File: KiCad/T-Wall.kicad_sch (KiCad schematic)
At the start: 62 parts, among them J1 IDC, J10 Conn_01x13, J2 IDC, J3 IDC, J4 IDC, J5 IDC, J6 IDC, J7 IDC, J8 IDC, J9 2086-1107/300-000/997-607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

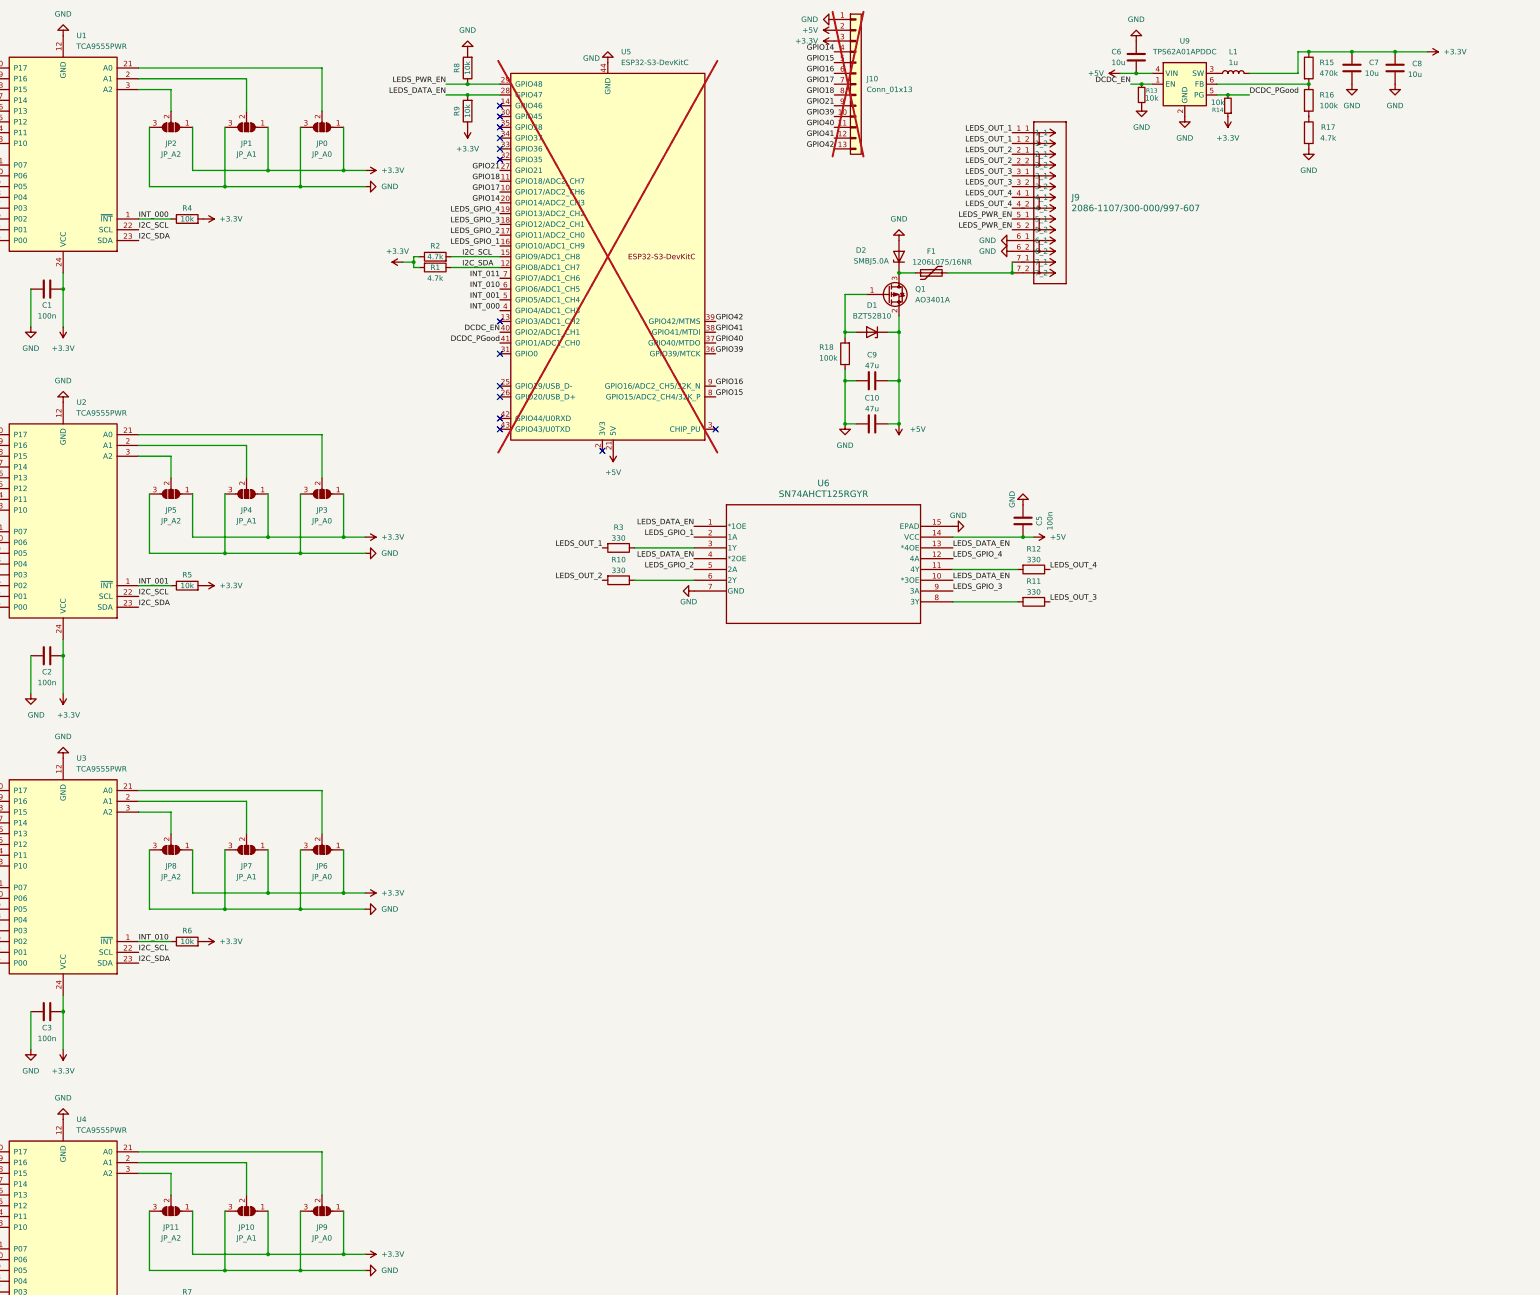
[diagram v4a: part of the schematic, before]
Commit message: PCB: finished for purchase at JLCPCB
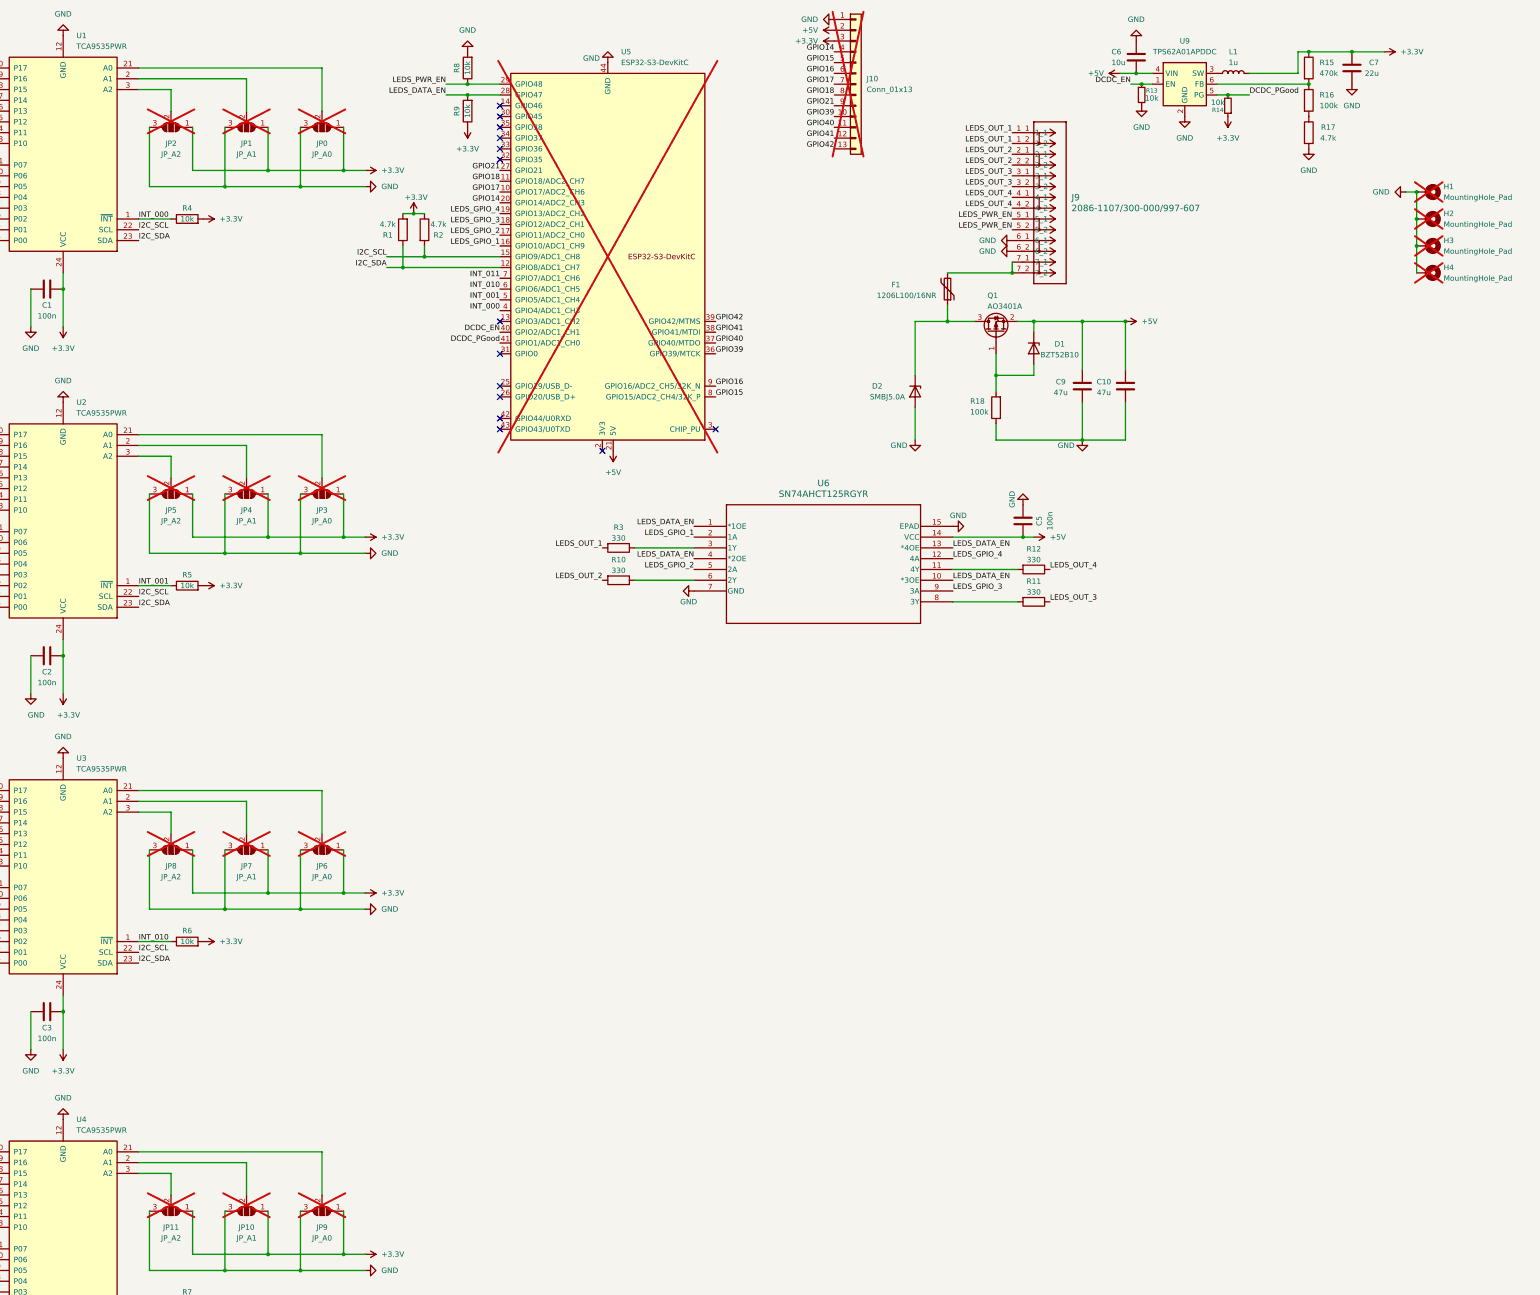
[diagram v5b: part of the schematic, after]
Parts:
- removed C8: 10u, Capacitor_SMD:C_1206_3216Metric_Pad1.33x1.80mm_HandSolder, symbol Device:C
- removed U1, U2, U3, U4: TCA9555PWR, Package_SO:TSSOP-24_4.4x7.8mm_P0.65mm, symbol Interface_Expansion:TCA9555PWR
- added H1, H2, H3, H4: MountingHole_Pad, MountingHole:MountingHole_3.2mm_M3_Pad_Via, symbol Mechanical:MountingHole_Pad
- added U1, U2, U3, U4: TCA9535PWR, Package_SO:TSSOP-24_4.4x7.8mm_P0.65mm, symbol Interface_Expansion:TCA9535PWR
- C7: value 10u -> 22u; LCSC C13585 -> C12891
- F1: value 1206L075/16NR -> 1206L100/16NR; LCSC C7542951 -> C7542956
- JP0, JP1, JP10, JP11, JP2, JP3, JP4, JP5, JP6, JP7, JP8, JP9: now not fitted
- L1: LCSC C1042 -> C6364732
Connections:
- net +3.3V: now also U1.24 (VCC), U2.24 (VCC), U3.24 (VCC), U4.24 (VCC)
- net GND: now also H1.1, H2.1, H3.1, H4.1, U1.12 (GND), U2.12 (GND), U3.12 (GND), U4.12 (GND)
- net I2C_SCL: now also U1.22 (SCL), U2.22 (SCL), U3.22 (SCL), U4.22 (SCL)
- net I2C_SDA: now also U1.23 (SDA), U2.23 (SDA), U3.23 (SDA), U4.23 (SDA)
- net INT_000: now also U1.1 (~{INT})
- net INT_001: now also U2.1 (~{INT})
- net INT_010: now also U3.1 (~{INT})
- net INT_011: now also U4.1 (~{INT})
- net Sensor_R1S1: now also U1.4 (P00)
- net Sensor_R1S2: now also U1.5 (P01)
- net Sensor_R1S3: now also U1.6 (P02)
- net Sensor_R1S4: now also U1.7 (P03)
- net Sensor_R1S5: now also U1.8 (P04)
- net Sensor_R1S6: now also U1.9 (P05)
- net Sensor_R1S7: now also U1.10 (P06)
- net Sensor_R1S8: now also U1.11 (P07)
- net Sensor_R2S1: now also U1.13 (P10)
- net Sensor_R2S2: now also U1.14 (P11)
- net Sensor_R2S3: now also U1.15 (P12)
- net Sensor_R2S4: now also U1.16 (P13)
- net Sensor_R2S5: now also U1.17 (P14)
- net Sensor_R2S6: now also U1.18 (P15)
- net Sensor_R2S7: now also U1.19 (P16)
- net Sensor_R2S8: now also U1.20 (P17)
- net Sensor_R3S1: now also U2.4 (P00)
- net Sensor_R3S2: now also U2.5 (P01)
- net Sensor_R3S3: now also U2.6 (P02)
- net Sensor_R3S4: now also U2.7 (P03)
- net Sensor_R3S5: now also U2.8 (P04)
- net Sensor_R3S6: now also U2.9 (P05)
- net Sensor_R3S7: now also U2.10 (P06)
- net Sensor_R3S8: now also U2.11 (P07)
- net Sensor_R4S1: now also U2.13 (P10)
- net Sensor_R4S2: now also U2.14 (P11)
- net Sensor_R4S3: now also U2.15 (P12)
- net Sensor_R4S4: now also U2.16 (P13)
- net Sensor_R4S5: now also U2.17 (P14)
- net Sensor_R4S6: now also U2.18 (P15)
- net Sensor_R4S7: now also U2.19 (P16)
- net Sensor_R4S8: now also U2.20 (P17)
- net Sensor_R5S1: now also U3.4 (P00)
- net Sensor_R5S2: now also U3.5 (P01)
- net Sensor_R5S3: now also U3.6 (P02)
- net Sensor_R5S4: now also U3.7 (P03)
- net Sensor_R5S5: now also U3.8 (P04)
- net Sensor_R5S6: now also U3.9 (P05)
- net Sensor_R5S7: now also U3.10 (P06)
- net Sensor_R5S8: now also U3.11 (P07)
- net Sensor_R6S1: now also U3.13 (P10)
- net Sensor_R6S2: now also U3.14 (P11)
- net Sensor_R6S3: now also U3.15 (P12)
- net Sensor_R6S4: now also U3.16 (P13)
- net Sensor_R6S5: now also U3.17 (P14)
- net Sensor_R6S6: now also U3.18 (P15)
- net Sensor_R6S7: now also U3.19 (P16)
- net Sensor_R6S8: now also U3.20 (P17)
- net Sensor_R7S1: now also U4.4 (P00)
- net Sensor_R7S2: now also U4.5 (P01)
- net Sensor_R7S3: now also U4.6 (P02)
- net Sensor_R7S4: now also U4.7 (P03)
- net Sensor_R7S5: now also U4.8 (P04)
- net Sensor_R7S6: now also U4.9 (P05)
- net Sensor_R7S7: now also U4.10 (P06)
- net Sensor_R7S8: now also U4.11 (P07)
- net Sensor_R8S1: now also U4.13 (P10)
- net Sensor_R8S2: now also U4.14 (P11)
- net Sensor_R8S3: now also U4.15 (P12)
- net Sensor_R8S4: now also U4.16 (P13)
- net Sensor_R8S5: now also U4.17 (P14)
- net Sensor_R8S6: now also U4.18 (P15)
- net Sensor_R8S7: now also U4.19 (P16)
- net Sensor_R8S8: now also U4.20 (P17)
- net at JP0.2 (C): now also U1.21 (A0)
- net at JP1.2 (C): now also U1.2 (A1)
- net at JP2.2 (C): now also U1.3 (A2)
- net at JP8.2 (C): now also U3.3 (A2)
- net at JP7.2 (C): now also U3.2 (A1)
- net at JP4.2 (C): now also U2.2 (A1)
- net at JP3.2 (C): now also U2.21 (A0)
- net at JP5.2 (C): now also U2.3 (A2)
- net at JP9.2 (C): now also U4.21 (A0)
- net at JP6.2 (C): now also U3.21 (A0)
- net at JP10.2 (C): now also U4.2 (A1)
- net at JP11.2 (C): now also U4.3 (A2)
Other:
- moved on the sheet: C10, C9, D1, D2, F1, Q1, R1, R18, R2
